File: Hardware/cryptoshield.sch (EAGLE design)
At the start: 41 parts, among them J1 AVR_SPI_PRG_6PTH, Q1 BSS138, Q2 BSS138, U1 33mhz

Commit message: more work done, still work in progress
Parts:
- removed SJ3: JUMPER-PAD-2-NOYES_SILK, SparkFun-Passives:JUMPER-PAD-2-NOYES_SILK
- added SJ1: JUMPER-PAD-2-NOYES_SILK, SparkFun-Passives:JUMPER-PAD-2-NOYES_SILK
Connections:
- removed net LV1: Q1.S, R3.2, SJ2.2
- removed net LV2: Q2.S, R1.2, SJ3.2
- new net N$4: SJ1.2, U$1.A4
- new net N$6: SJ2.2, U$1.A5
- net SCL: now also Q2.S, R1.2; no longer SJ3.1
- net SCL_IN: now also SJ2.1
- net SDA: now also Q1.S, R3.2; no longer SJ2.1
- net SDA_IN: now also SJ1.1
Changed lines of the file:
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@@
 <part name="SUPPLY2" library="SparkFun-Aesthetics" deviceset="3.3V" device=""/>
 <part name="SUPPLY3" library="SparkFun-Aesthetics" deviceset="5V" device=""/>
-<part name="SJ2" library="SparkFun-Passives" deviceset="JUMPER-PAD-2-NO" device="YES_SILK"/>
 <part name="Q2" library="SparkFun-DiscreteSemi" deviceset="MOSFET-NCHANNEL" device="BSS138" value="BSS138"/>
 <part name="R1" library="SparkFun" deviceset="RESISTOR" device="0603-RES" value="10K"/>
@@
 <part name="SUPPLY5" library="SparkFun-Aesthetics" deviceset="3.3V" device=""/>
 <part name="SUPPLY8" library="SparkFun-Aesthetics" deviceset="5V" device=""/>
-<part name="SJ3" library="SparkFun-Passives" deviceset="JUMPER-PAD-2-NO" device="YES_SILK"/>
 <part name="U$8" library="SparkFun-RF" deviceset="ID-12/20" device="SMD"/>
 <part name="SUPPLY18" library="SparkFun-Aesthetics" deviceset="3.3V" device=""/>
@@
 <part name="GND9" library="SparkFun-Aesthetics" deviceset="GND" device=""/>
 <part name="JP2" library="SparkFun-Connectors" deviceset="M03" device="PTH"/>
+<part name="SJ1" library="SparkFun-Passives" deviceset="JUMPER-PAD-2-NO" device="YES_SILK" value=""/>
+<part name="SJ2" library="SparkFun-Passives" deviceset="JUMPER-PAD-2-NO" device="YES_SILK" value=""/>
 </parts>
 <sheets>
@@
 <instance part="SUPPLY2" gate="G$1" x="317.5" y="165.1"/>
 <instance part="SUPPLY3" gate="G$1" x="332.74" y="165.1"/>
-<instance part="SJ2" gate="G$1" x="309.88" y="147.32" smashed="yes"/>
 <instance part="Q2" gate="G$1" x="388.62" y="157.48" smashed="yes" rot="R270">
 <attribute name="NAME" x="384.81" y="162.306" size="1.778" layer="95"/>
@@
 <instance part="SUPPLY5" gate="G$1" x="381" y="175.26"/>
 <instance part="SUPPLY8" gate="G$1" x="396.24" y="175.26"/>
-<instance part="SJ3" gate="G$1" x="373.38" y="157.48" smashed="yes"/>
 <instance part="U$8" gate="G$1" x="60.96" y="154.94"/>
 <instance part="SUPPLY18" gate="G$1" x="35.56" y="172.72"/>
@@
 <instance part="GND9" gate="1" x="109.22" y="139.7"/>
 <instance part="JP2" gate="G$1" x="121.92" y="45.72" rot="R180"/>
+<instance part="SJ1" gate="G$1" x="30.48" y="251.46"/>
+<instance part="SJ2" gate="G$1" x="22.86" y="248.92"/>
 </instances>
 <busses>
@@
 </segment>
 <segment>
-<pinref part="SJ3" gate="G$1" pin="1"/>
-<wire x1="368.3" y1="157.48" x2="365.76" y2="157.48" width="0.1524" layer="91"/>
+<wire x1="381" y1="157.48" x2="365.76" y2="157.48" width="0.1524" layer="91"/>
 <label x="365.76" y="157.48" size="1.27" layer="95" rot="R180" xref="yes"/>
+<wire x1="383.54" y1="157.48" x2="381" y2="157.48" width="0.1524" layer="91"/>
+<wire x1="381" y1="160.02" x2="381" y2="157.48" width="0.1524" layer="91"/>
+<pinref part="Q2" gate="G$1" pin="S"/>
+<pinref part="R1" gate="G$1" pin="2"/>
+<junction x="381" y="157.48"/>
 </segment>
 <segment>
@@
 </segment>
 <segment>
-<pinref part="SJ2" gate="G$1" pin="1"/>
-<wire x1="304.8" y1="147.32" x2="302.26" y2="147.32" width="0.1524" layer="91"/>
+<wire x1="317.5" y1="147.32" x2="302.26" y2="147.32" width="0.1524" layer="91"/>
 <label x="302.26" y="147.32" size="1.27" layer="95" rot="R180" xref="yes"/>
+<wire x1="320.04" y1="147.32" x2="317.5" y2="147.32" width="0.1524" layer="91"/>
+<wire x1="317.5" y1="149.86" x2="317.5" y2="147.32" width="0.1524" layer="91"/>
+<pinref part="Q1" gate="G$1" pin="S"/>
+<pinref part="R3" gate="G$1" pin="2"/>
+<junction x="317.5" y="147.32"/>
 </segment>
 <segment>
@@
 </segment>
 </net>
-<net name="LV1" class="0">
-<segment>
-<wire x1="320.04" y1="147.32" x2="317.5" y2="147.32" width="0.1524" layer="91"/>
-<wire x1="317.5" y1="147.32" x2="314.96" y2="147.32" width="0.1524" layer="91"/>
-<wire x1="317.5" y1="149.86" x2="317.5" y2="147.32" width="0.1524" layer="91"/>
-<junction x="317.5" y="147.32"/>
-<pinref part="Q1" gate="G$1" pin="S"/>
-<pinref part="R3" gate="G$1" pin="2"/>
-<pinref part="SJ2" gate="G$1" pin="2"/>
-</segment>
-</net>
 <net name="5V" class="0">
 <segment>
@@
 <label x="340.36" y="147.32" size="1.27" layer="95" xref="yes"/>
 </segment>
+<segment>
+<pinref part="SJ1" gate="G$1" pin="1"/>
+<wire x1="25.4" y1="251.46" x2="15.24" y2="251.46" width="0.1524" layer="91"/>
+<label x="15.24" y="251.46" size="1.27" layer="95" rot="R180" xref="yes"/>
+</segment>
 </net>
 <net name="SCL_IN" class="0">
@@
 <label x="403.86" y="157.48" size="1.27" layer="95" xref="yes"/>
 </segment>
-</net>
-<net name="LV2" class="0">
-<segment>
-<wire x1="383.54" y1="157.48" x2="381" y2="157.48" width="0.1524" layer="91"/>
-<wire x1="381" y1="157.48" x2="378.46" y2="157.48" width="0.1524" layer="91"/>
-<wire x1="381" y1="160.02" x2="381" y2="157.48" width="0.1524" layer="91"/>
-<junction x="381" y="157.48"/>
-<pinref part="Q2" gate="G$1" pin="S"/>
-<pinref part="R1" gate="G$1" pin="2"/>
-<pinref part="SJ3" gate="G$1" pin="2"/>
+<segment>
+<pinref part="SJ2" gate="G$1" pin="1"/>
+<wire x1="17.78" y1="248.92" x2="15.24" y2="248.92" width="0.1524" layer="91"/>
+<label x="15.24" y="248.92" size="1.27" layer="95" rot="R180" xref="yes"/>
 </segment>
 </net>
@@
 </segment>
 </net>
+<net name="N$4" class="0">
+<segment>
+<pinref part="U$1" gate="G$1" pin="A4"/>
+<pinref part="SJ1" gate="G$1" pin="2"/>
+<wire x1="35.56" y1="251.46" x2="50.8" y2="251.46" width="0.1524" layer="91"/>
+</segment>
+</net>
+<net name="N$6" class="0">
+<segment>
+<pinref part="U$1" gate="G$1" pin="A5"/>
+<pinref part="SJ2" gate="G$1" pin="2"/>
+<wire x1="27.94" y1="248.92" x2="50.8" y2="248.92" width="0.1524" layer="91"/>
+</segment>
+</net>

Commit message: finished layout, ready for review
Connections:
- net 3.3V: no longer C1.1, C10.1, U$8.5V, U$8.RES
- net 5V: now also C1.1, C10.1, U$8.5V, U$8.RES
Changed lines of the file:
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@@
 <part name="SUPPLY6" library="SparkFun-Aesthetics" deviceset="3.3V" device=""/>
 <part name="SUPPLY7" library="SparkFun-Aesthetics" deviceset="3.3V" device=""/>
-<part name="SUPPLY11" library="SparkFun-Aesthetics" deviceset="3.3V" device=""/>
 <part name="SHA1" library="cryptotronix" deviceset="ATSHA204" device=""/>
 <part name="SUPPLY14" library="SparkFun-Aesthetics" deviceset="3.3V" device=""/>
@@
 <part name="SUPPLY8" library="SparkFun-Aesthetics" deviceset="5V" device=""/>
 <part name="U$8" library="SparkFun-RF" deviceset="ID-12/20" device="SMD"/>
-<part name="SUPPLY18" library="SparkFun-Aesthetics" deviceset="3.3V" device=""/>
 <part name="S1" library="SparkFun-Electromechanical" deviceset="TAC_SWITCH" device="SMD"/>
 <part name="GND6" library="SparkFun-Aesthetics" deviceset="GND" device=""/>
@@
 <part name="C1" library="SparkFun-Capacitors" deviceset="10UF50V20%(1210)" device="" value="10uF"/>
 <part name="C10" library="SparkFun-Passives" deviceset="CAP" device="0603-CAP" value="1000uF"/>
-<part name="SUPPLY25" library="SparkFun-Aesthetics" deviceset="3.3V" device=""/>
-<part name="SUPPLY26" library="SparkFun-Aesthetics" deviceset="3.3V" device=""/>
 <part name="GND8" library="SparkFun-Aesthetics" deviceset="GND" device=""/>
 <part name="GND9" library="SparkFun-Aesthetics" deviceset="GND" device=""/>
@@
 <part name="SJ1" library="SparkFun-Passives" deviceset="JUMPER-PAD-2-NO" device="YES_SILK" value=""/>
 <part name="SJ2" library="SparkFun-Passives" deviceset="JUMPER-PAD-2-NO" device="YES_SILK" value=""/>
+<part name="SUPPLY1" library="SparkFun-Aesthetics" deviceset="5V" device=""/>
+<part name="SUPPLY4" library="SparkFun-Aesthetics" deviceset="5V" device=""/>
+<part name="SUPPLY11" library="SparkFun-Aesthetics" deviceset="5V" device=""/>
+<part name="SUPPLY18" library="SparkFun-Aesthetics" deviceset="5V" device=""/>
 </parts>
 <sheets>
@@
 <instance part="SUPPLY6" gate="G$1" x="40.64" y="43.18"/>
 <instance part="SUPPLY7" gate="G$1" x="190.5" y="45.72"/>
-<instance part="SUPPLY11" gate="G$1" x="78.74" y="172.72"/>
 <instance part="SHA1" gate="G$1" x="175.26" y="93.98"/>
 <instance part="SUPPLY14" gate="G$1" x="195.58" y="104.14"/>
@@
 <instance part="SUPPLY8" gate="G$1" x="396.24" y="175.26"/>
 <instance part="U$8" gate="G$1" x="60.96" y="154.94"/>
-<instance part="SUPPLY18" gate="G$1" x="35.56" y="172.72"/>
 <instance part="S1" gate="S" x="35.56" y="20.32"/>
 <instance part="GND6" gate="1" x="25.4" y="10.16"/>
@@
 <instance part="C1" gate="G$1" x="12.7" y="154.94"/>
 <instance part="C10" gate="G$1" x="109.22" y="152.4"/>
-<instance part="SUPPLY25" gate="G$1" x="12.7" y="172.72"/>
-<instance part="SUPPLY26" gate="G$1" x="109.22" y="170.18"/>
 <instance part="GND8" gate="1" x="12.7" y="137.16"/>
 <instance part="GND9" gate="1" x="109.22" y="139.7"/>
@@
 <instance part="SJ1" gate="G$1" x="30.48" y="251.46"/>
 <instance part="SJ2" gate="G$1" x="22.86" y="248.92"/>
+<instance part="SUPPLY1" gate="G$1" x="35.56" y="172.72"/>
+<instance part="SUPPLY4" gate="G$1" x="78.74" y="172.72"/>
+<instance part="SUPPLY11" gate="G$1" x="12.7" y="172.72"/>
+<instance part="SUPPLY18" gate="G$1" x="109.22" y="170.18"/>
 </instances>
 <busses>
@@
 </segment>
 <segment>
-<wire x1="78.74" y1="172.72" x2="78.74" y2="162.56" width="0.1524" layer="91"/>
-<pinref part="SUPPLY11" gate="G$1" pin="3.3V"/>
-<pinref part="U$8" gate="G$1" pin="5V"/>
-<wire x1="76.2" y1="162.56" x2="78.74" y2="162.56" width="0.1524" layer="91"/>
-</segment>
-<segment>
 <wire x1="304.8" y1="236.22" x2="304.8" y2="233.68" width="0.1524" layer="91"/>
 <pinref part="C13" gate="G$1" pin="1"/>
@@
 </segment>
 <segment>
-<pinref part="U$8" gate="G$1" pin="RES"/>
-<wire x1="45.72" y1="154.94" x2="35.56" y2="154.94" width="0.1524" layer="91"/>
-<wire x1="35.56" y1="154.94" x2="35.56" y2="172.72" width="0.1524" layer="91"/>
-<pinref part="SUPPLY18" gate="G$1" pin="3.3V"/>
-</segment>
-<segment>
 <wire x1="251.46" y1="167.64" x2="264.16" y2="167.64" width="0.1524" layer="91"/>
 <pinref part="SUPPLY19" gate="G$1" pin="3.3V"/>
@@
 <pinref part="JP4" gate="G$1" pin="6"/>
 </segment>
-<segment>
-<pinref part="C1" gate="G$1" pin="1"/>
-<pinref part="SUPPLY25" gate="G$1" pin="3.3V"/>
-<wire x1="12.7" y1="160.02" x2="12.7" y2="172.72" width="0.1524" layer="91"/>
-</segment>
-<segment>
-<pinref part="C10" gate="G$1" pin="1"/>
-<pinref part="SUPPLY26" gate="G$1" pin="3.3V"/>
-<wire x1="109.22" y1="157.48" x2="109.22" y2="170.18" width="0.1524" layer="91"/>
-</segment>
 </net>
 <net name="32KHZ" class="0">
@@
 <wire x1="38.1" y1="233.68" x2="38.1" y2="269.24" width="0.1524" layer="91"/>
 </segment>
-</net>
+<segment>
+<pinref part="U$8" gate="G$1" pin="RES"/>
+<wire x1="45.72" y1="154.94" x2="35.56" y2="154.94" width="0.1524" layer="91"/>
+<wire x1="35.56" y1="154.94" x2="35.56" y2="172.72" width="0.1524" layer="91"/>
+<pinref part="SUPPLY1" gate="G$1" pin="5V"/>
+</segment>
+<segment>
+<wire x1="78.74" y1="172.72" x2="78.74" y2="162.56" width="0.1524" layer="91"/>
+<pinref part="U$8" gate="G$1" pin="5V"/>
+<wire x1="76.2" y1="162.56" x2="78.74" y2="162.56" width="0.1524" layer="91"/>
+<pinref part="SUPPLY4" gate="G$1" pin="5V"/>
+</segment>
+<segment>
+<pinref part="C1" gate="G$1" pin="1"/>
+<wire x1="12.7" y1="160.02" x2="12.7" y2="172.72" width="0.1524" layer="91"/>
+<pinref part="SUPPLY11" gate="G$1" pin="5V"/>
+</segment>
+<segment>
+<pinref part="C10" gate="G$1" pin="1"/>
+<wire x1="109.22" y1="157.48" x2="109.22" y2="170.18" width="0.1524" layer="91"/>
+<pinref part="SUPPLY18" gate="G$1" pin="5V"/>
+</segment>
+</net>

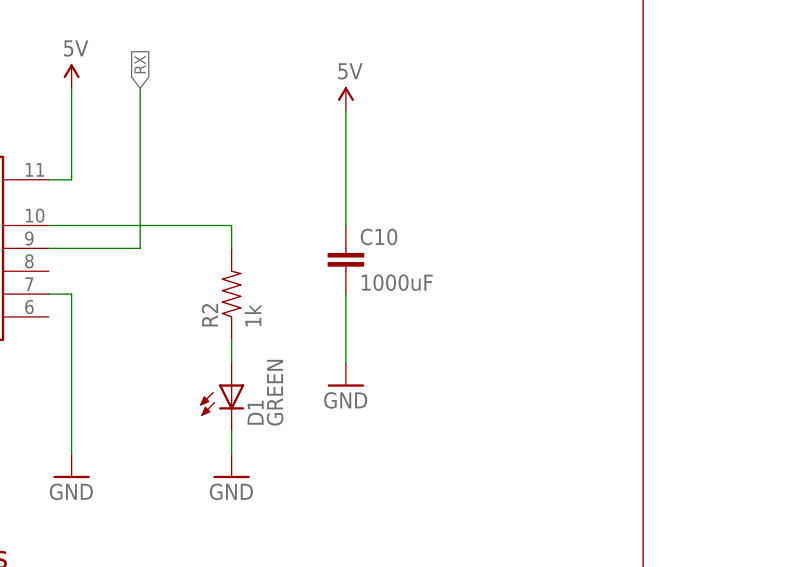
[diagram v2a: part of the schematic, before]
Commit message: changed name of part
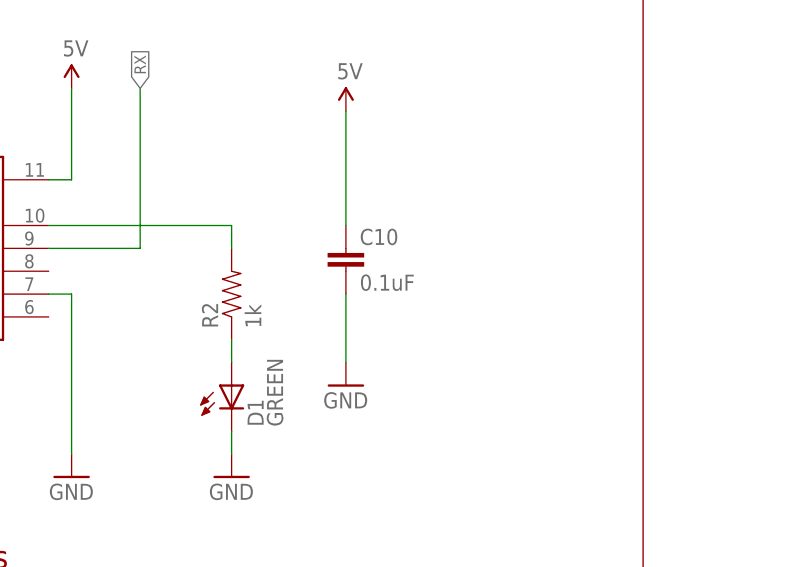
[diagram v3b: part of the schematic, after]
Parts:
- C10: value 1000uF -> 0.1uF; device SparkFun-Passives:CAP0603-CAP -> SparkFun-Capacitors:0.1UF-25V(+80/-20%)(0603)
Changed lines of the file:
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@@
 <part name="JP4" library="SparkFun-Connectors" deviceset="M06" device="NO_SILK"/>
 <part name="C1" library="SparkFun-Capacitors" deviceset="10UF50V20%(1210)" device="" value="10uF"/>
-<part name="C10" library="SparkFun-Passives" deviceset="CAP" device="0603-CAP" value="1000uF"/>
+<part name="C10" library="SparkFun-Capacitors" deviceset="0.1UF-25V(+80/-20%)(0603)" device="" value="0.1uF"/>
 <part name="GND8" library="SparkFun-Aesthetics" deviceset="GND" device=""/>
 <part name="GND9" library="SparkFun-Aesthetics" deviceset="GND" device=""/>
